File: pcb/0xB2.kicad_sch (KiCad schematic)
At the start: 40 parts, among them J1 USB_C_Receptacle_USB2.0, J2 Conn_01x12, J3 Conn_01x05, J4 Conn_01x12, J5 Conn_01x02, SW1 SW_Push, SW2 SW_Push, U1 RP2040, U2 GD25Q80CEIGR, U3 XC6210B332MR-G, Y1 Crystal_GND24

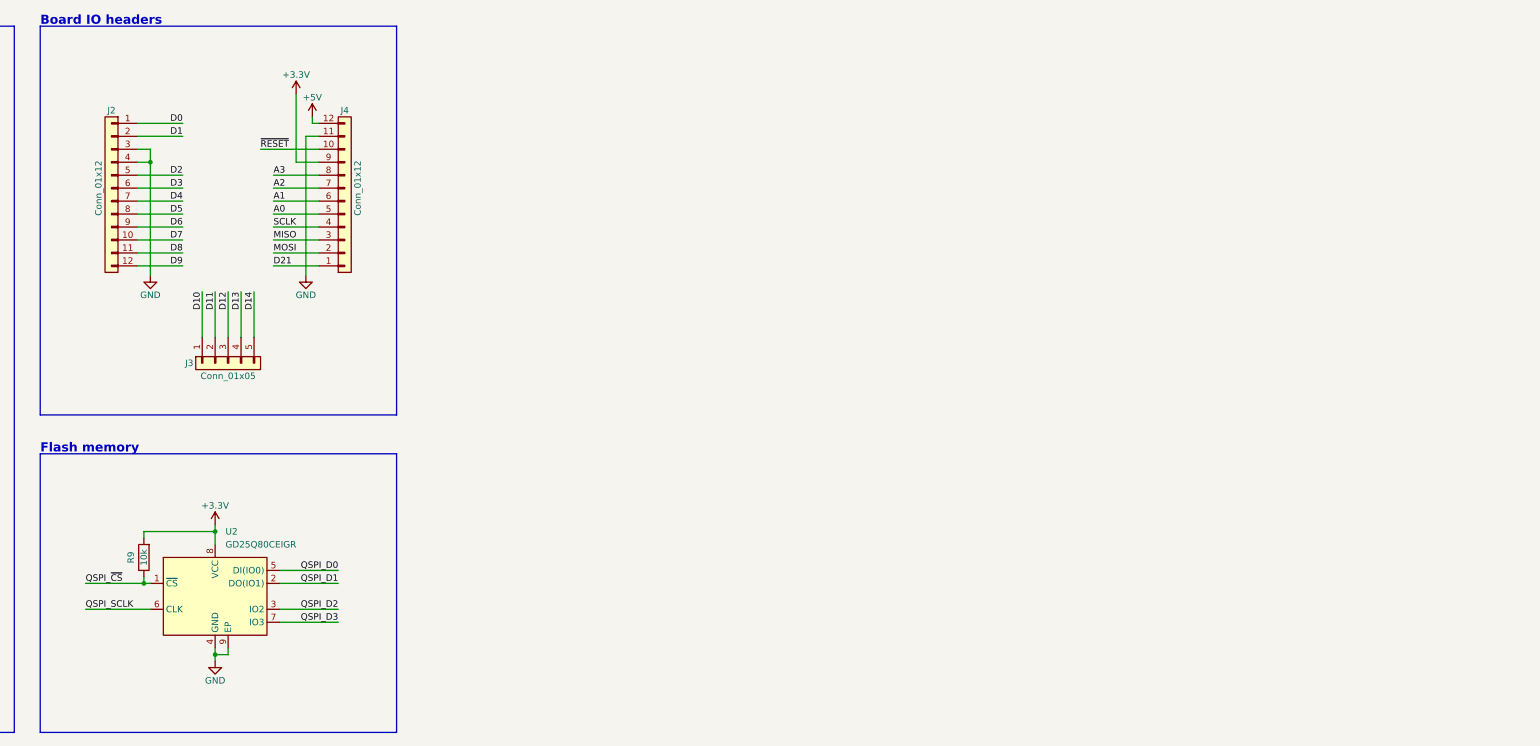
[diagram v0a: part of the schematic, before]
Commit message: add headers
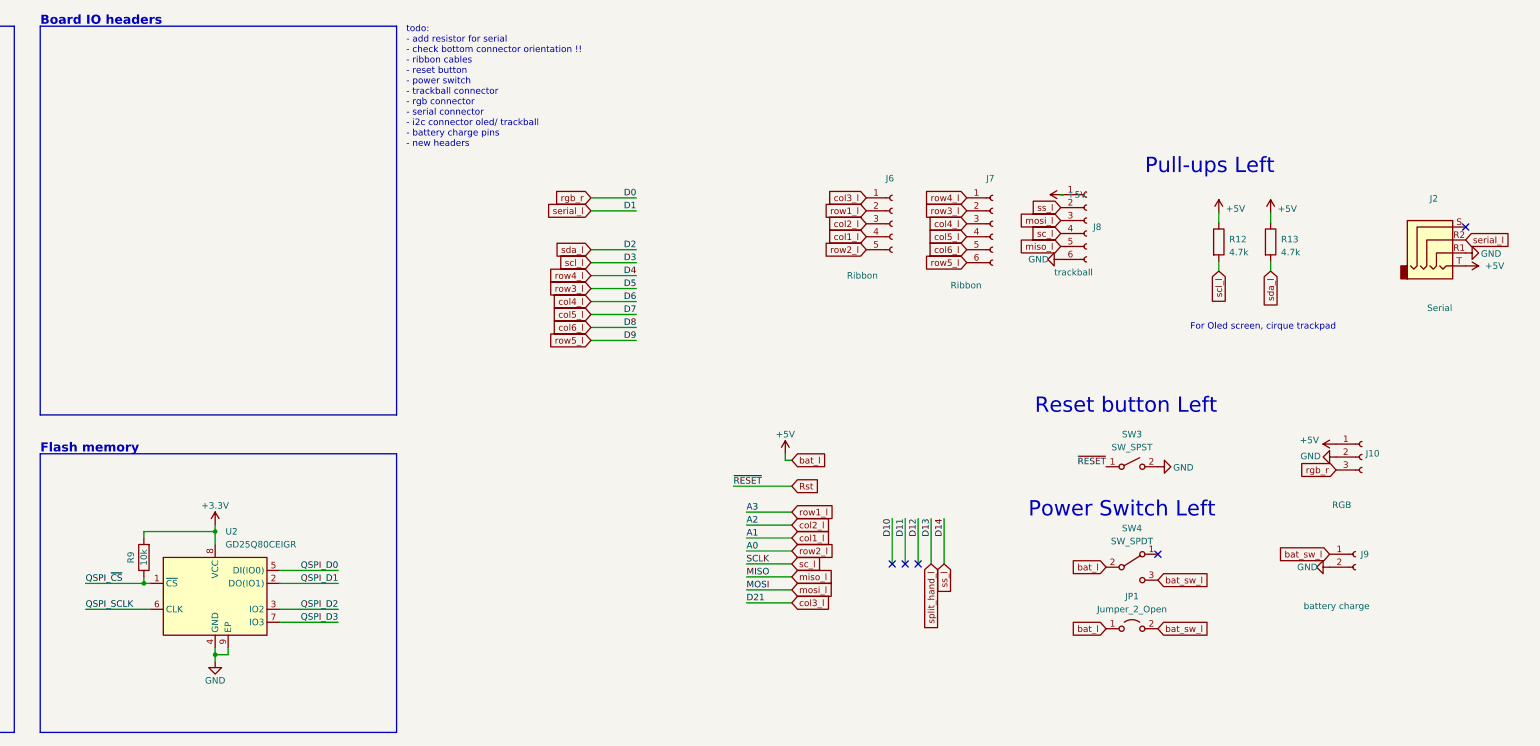
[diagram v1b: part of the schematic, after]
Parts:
- removed J2, J4: Conn_01x12, 0xLib_Connectors:PinHeader_1x12_P2.54mm, symbol Connector_Generic:Conn_01x12
- removed J3: Conn_01x05, 0xLib_Connectors:PinHeader_1x05_P2.54mm, symbol Connector_Generic:Conn_01x05
- added J10: RGB, Connector_PinHeader_2.54mm:PinHeader_1x03_P2.54mm_Vertical, symbol Connector:Conn_01x03_Female
- added J2: Serial, 0xB2_drawings:Jack_3.5mm_PJ320E_Horizontal, symbol Connector:AudioJack4
- added J6: Ribbon, Connector_PinHeader_2.54mm:PinHeader_1x05_P2.54mm_Vertical, symbol Connector:Conn_01x05_Female
- added J7: Ribbon, Connector_PinHeader_2.54mm:PinHeader_1x06_P2.54mm_Vertical, symbol Connector:Conn_01x06_Female
- added J8: trackball, Connector_PinHeader_2.54mm:PinHeader_1x06_P2.54mm_Vertical, symbol Connector:Conn_01x06_Female
- added J9: battery charge, Connector_PinHeader_2.54mm:PinHeader_1x02_P2.54mm_Vertical, symbol Connector:Conn_01x02_Female
- added JP1: Jumper_2_Open, Library:power_switch_jumper, symbol Jumper:Jumper_2_Open
- added R12, R13: 4.7k, Library:R_1206_handsolder, symbol Device:R
- added SW3: SW_SPST, Library:PushSwitch, symbol Switch:SW_SPST
- added SW4: SW_SPDT, Library:SW_SPDT+H-MSK12C01_hor(7pin_SMD), symbol Switch:SW_SPDT
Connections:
- net +5V: now also J10.1 (Pin_1), J2.T, J8.1 (Pin_1), JP1.1 (A), R12.1, R13.1, SW4.2 (B)
- net GND: now also J10.2 (Pin_2), J2.R1, J8.6 (Pin_6), J9.2 (Pin_2), SW3.2 (B)
- net A0 renamed row2_l
- net row2_l: now also J6.5 (Pin_5)
- net A1 renamed col1_l
- net col1_l: now also J6.4 (Pin_4)
- net A2 renamed col2_l
- net col2_l: now also J6.3 (Pin_3)
- net A3 renamed row1_l
- net row1_l: now also J6.2 (Pin_2)
- net D0 renamed rgb_r
- net rgb_r: now also J10.3 (Pin_3)
- net D1 renamed serial_l
- net serial_l: now also J2.R2
- net D13 renamed split_hand_l
- net D14 renamed ss_l
- net ss_l: now also J8.2 (Pin_2)
- net D2 renamed sda_l
- net sda_l: now also R13.2
- net D21 renamed col3_l
- net col3_l: now also J6.1 (Pin_1)
- net D3 renamed scl_l
- net scl_l: now also R12.2
- net D4 renamed row4_l
- net row4_l: now also J7.1 (Pin_1)
- net D5 renamed row3_l
- net row3_l: now also J7.2 (Pin_2)
- net D6 renamed col4_l
- net col4_l: now also J7.3 (Pin_3)
- net D7 renamed col5_l
- net col5_l: now also J7.4 (Pin_4)
- net D8 renamed col6_l
- net col6_l: now also J7.5 (Pin_5)
- net D9 renamed row5_l
- net row5_l: now also J7.6 (Pin_6)
- net MISO renamed miso_l
- net miso_l: now also J8.5 (Pin_5)
- net MOSI renamed mosi_l
- net mosi_l: now also J8.3 (Pin_3)
- net SCLK renamed sc_l
- net sc_l: now also J8.4 (Pin_4)
- net ~{RESET} renamed Rst
- net Rst: now also SW3.1 (A)
- new net bat_sw_l: J9.1 (Pin_1), JP1.2 (B), SW4.3 (C)
- no-connect marks 9 -> 14
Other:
- note added: "For Oled screen, cirque trackpad"
- note added: "Power Switch Left"
- note added: "Pull-ups Left"
- note added: "Reset button Left"
- note added: "todo: - add resistor for serial - check bottom connector orientation !! - ribbon cables - reset button - power switch - trackball connector - rgb connector - serial connector - i2c connector oled/ trackball - battery charge pins - new headers"

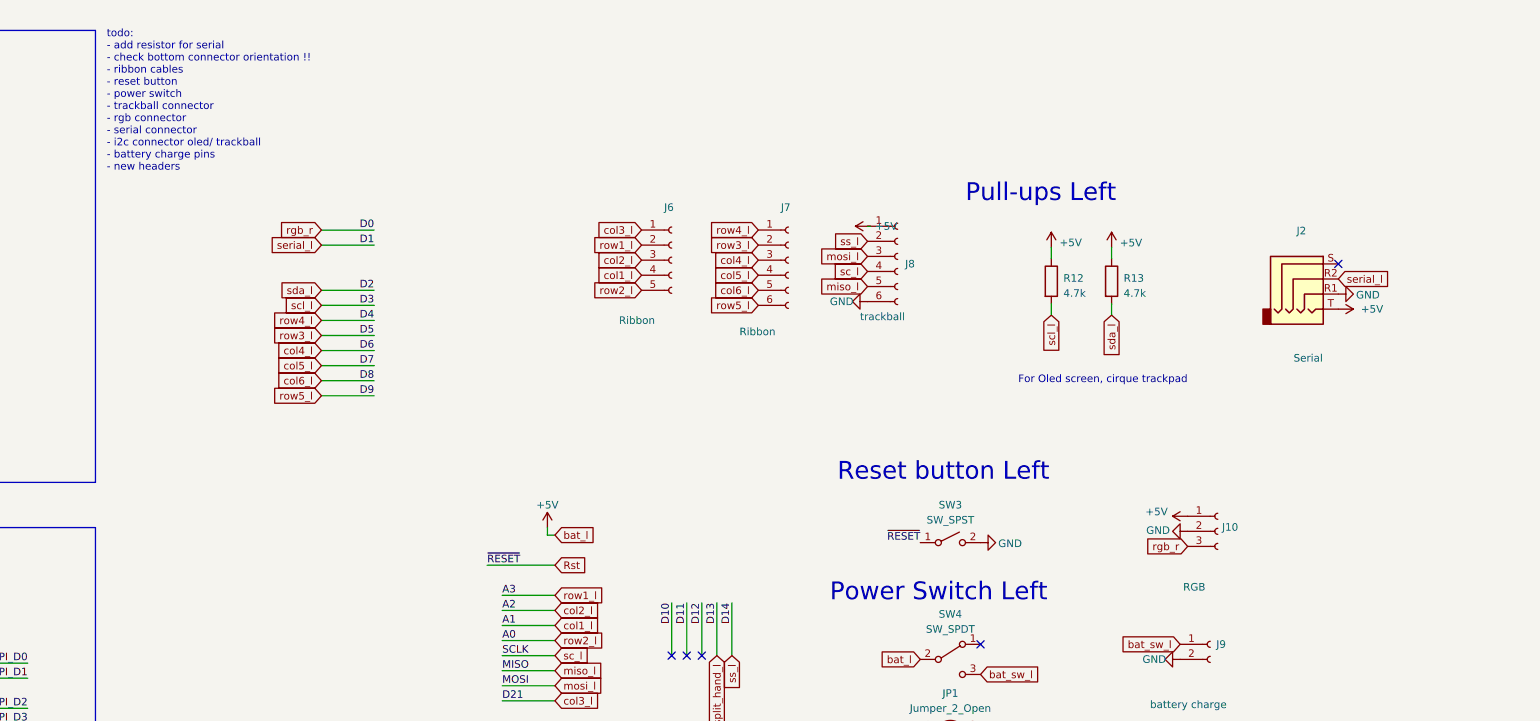
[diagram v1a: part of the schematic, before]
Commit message: add resistors
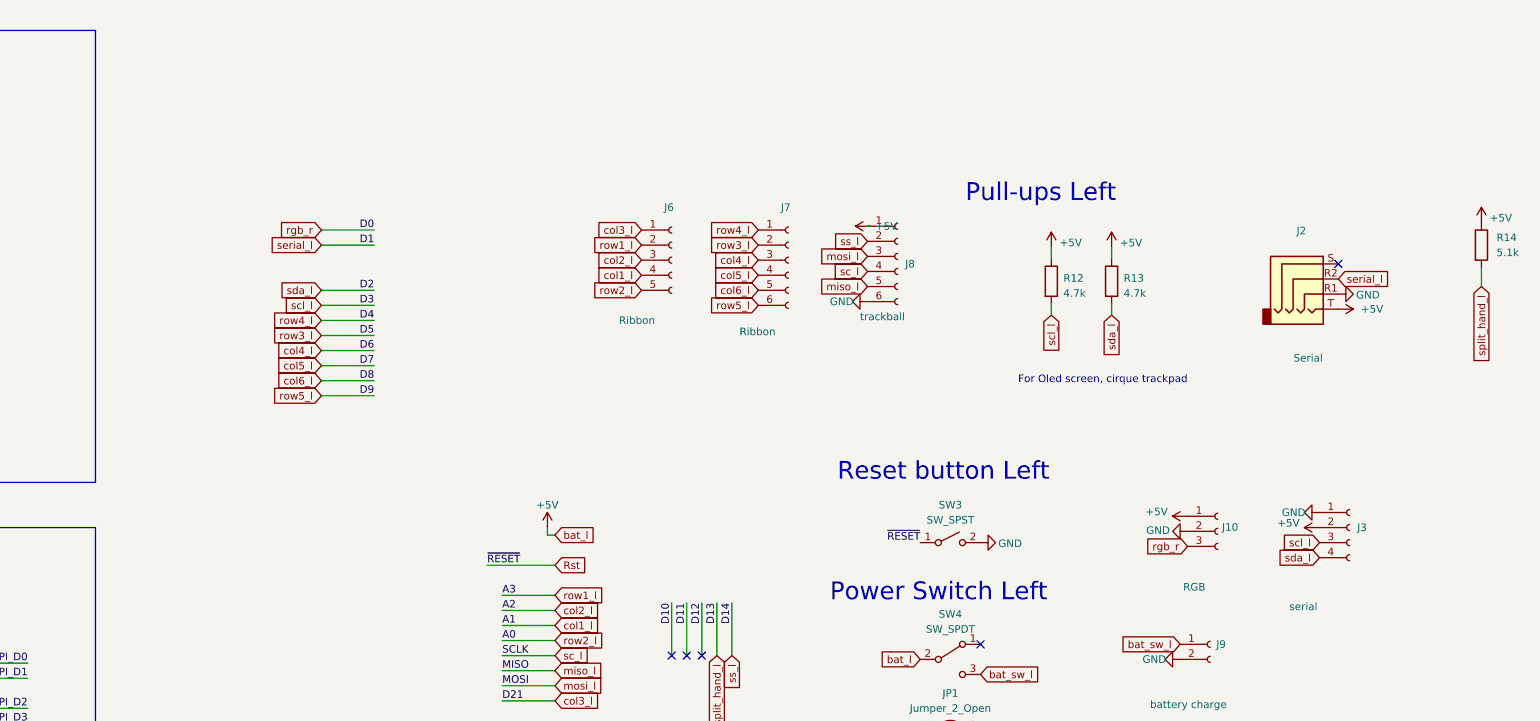
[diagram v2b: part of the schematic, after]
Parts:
- added J3: serial, Connector_PinHeader_2.54mm:PinHeader_1x04_P2.54mm_Vertical, symbol Connector:Conn_01x04_Female
- added R14: 5.1k, Resistor_SMD:R_0402_1005Metric, symbol Device:R
- R12, R13: footprint Library:R_1206_handsolder -> Resistor_SMD:R_0402_1005Metric
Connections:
- net +5V: now also J3.2 (Pin_2), R14.1
- net GND: now also J3.1 (Pin_1)
- net scl_l: now also J3.3 (Pin_3)
- net sda_l: now also J3.4 (Pin_4)
- net split_hand_l: now also R14.2
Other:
- note removed: "todo: - add resistor for serial - check bottom connector orientation !! - ribbon cables - reset button - power switch - trackball connector - rgb connector - serial connector - i2c connector oled/ trackball - battery charge pins - new headers"
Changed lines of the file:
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@@
+    (stroke (width 0) (type default) (color 0 0 0 0))
+  )
+  (wire (pts (xy 513.08 60.325) (xy 513.08 63.5))
     (stroke (width 0) (type default) (color 0 0 0 0))
   )
@@
   (text "Voltage regulation" (at 17.78 96.52 0)
     (effects (font (size 1.778 1.778) (thickness 0.3556) bold) (justify left bottom))
-  )
-  (text "todo:\n- add resistor for serial\n- check bottom connector orientation !!\n- ribbon cables\n- reset button\n- power switch\n- trackball connector \n- rgb connector\n- serial connector\n- i2c connector oled/ trackball\n- battery charge pins\n- new headers"
-    (at 281.305 44.196 0)
-    (effects (font (size 1.27 1.27)) (justify left bottom))
   )
   (text "Reset button Left" (at 404.495 96.52 0)
@@
     )
   )
+  (global_label "scl_l" (shape input) (at 485.775 106.68 180)
+    (effects (font (size 1.27 1.27)) (justify right))
+    (property "Intersheet References" "${INTERSHEET_REFS}" (id 0) (at 456.565 52.07 0)
+      (effects (font (size 1.27 1.27)) hide)
+    )
+  )
   (global_label "row1_l" (shape input) (at 371.475 56.515 180)
     (effects (font (size 1.27 1.27)) (justify right))
@@
     )
   )
+  (global_label "split_hand_l" (shape input) (at 513.08 63.5 270)
+    (effects (font (size 1.27 1.27)) (justify right))
+    (property "Intersheet References" "${INTERSHEET_REFS}" (id 0) (at 513.1594 75.6498 90)
+      (effects (font (size 1.27 1.27)) (justify right) hide)
+    )
+  )
   (global_label "bat_sw_l" (shape input) (at 428.625 138.43 0)
     (effects (font (size 1.27 1.27)) (justify left))
@@
     (property "Intersheet References" "${INTERSHEET_REFS}" (id 0) (at 405.1057 55.8006 0)
       (effects (font (size 1.27 1.27)) (justify right) hide)
+    )
+  )
+  (global_label "sda_l" (shape input) (at 485.775 109.22 180)
+    (effects (font (size 1.27 1.27)) (justify right))
+    (property "Intersheet References" "${INTERSHEET_REFS}" (id 0) (at 456.565 54.61 0)
+      (effects (font (size 1.27 1.27)) hide)
     )
   )
@@
       (effects (font (size 1.27 1.27)) hide)
     )
+  )
+  (symbol (lib_id "power:+5V") (at 485.775 104.14 90) (unit 1)
+    (in_bom yes) (on_board yes)
+    (property "Reference" "#PWR0115" (id 0) (at 489.585 104.14 0)
+      (effects (font (size 1.27 1.27)) hide)
+    )
+    (property "Value" "+5V" (id 1) (at 478.663 103.378 90)
+      (effects (font (size 1.27 1.27)) (justify right))
+    )
+    (property "Footprint" "" (id 2) (at 485.775 104.14 0)
+      (effects (font (size 1.27 1.27)) hide)
+    )
+    (property "Datasheet" "" (id 3) (at 485.775 104.14 0)
+      (effects (font (size 1.27 1.27)) hide)
+    )
+    (pin "1")
   )
   (symbol (lib_id "Device:C") (at 148.59 180.34 0) (unit 1)
@@
       (effects (font (size 1.27 1.27)) (justify left))
     )
-    (property "Footprint" "Library:R_1206_handsolder" (id 2) (at 438.785 62.611 90)
+    (property "Footprint" "Resistor_SMD:R_0402_1005Metric" (id 2) (at 438.785 62.611 90)
       (effects (font (size 1.27 1.27)) hide)
     )
@@
     (pin "2")
   )
+  (symbol (lib_id "Connector:Conn_01x04_Female") (at 490.855 104.14 0) (unit 1)
+    (in_bom yes) (on_board yes)
+    (property "Reference" "J3" (id 0) (at 492.125 104.1399 0)
+      (effects (font (size 1.27 1.27)) (justify left))
+    )
+    (property "Value" "serial" (id 1) (at 480.695 117.475 0)
+      (effects (font (size 1.27 1.27)) (justify left))
+    )
+    (property "Footprint" "Connector_PinHeader_2.54mm:PinHeader_1x04_P2.54mm_Vertical" (id 2) (at 490.855 104.14 0)
+      (effects (font (size 1.27 1.27)) hide)
+    )
+    (property "Datasheet" "~" (id 3) (at 490.855 104.14 0)
+      (effects (font (size 1.27 1.27)) hide)
+    )
+    (pin "1")
+    (pin "2")
+    (pin "3")
+    (pin "4")
+  )
   (symbol (lib_id "Device:R") (at 24.765 181.61 180) (unit 1)
     (in_bom yes) (on_board yes)
@@
     (pin "1")
   )
+  (symbol (lib_id "power:GND") (at 485.775 101.6 270) (unit 1)
+    (in_bom yes) (on_board yes)
+    (property "Reference" "#PWR0114" (id 0) (at 479.425 101.6 0)
+      (effects (font (size 1.27 1.27)) hide)
+    )
+    (property "Value" "GND" (id 1) (at 479.425 101.6 90)
+      (effects (font (size 1.27 1.27)) (justify left))
+    )
+    (property "Footprint" "" (id 2) (at 485.775 101.6 0)
+      (effects (font (size 1.27 1.27)) hide)
+    )
+    (property "Datasheet" "" (id 3) (at 485.775 101.6 0)
+      (effects (font (size 1.27 1.27)) hide)
+    )
+    (pin "1")
+  )
   (symbol (lib_id "Device:R") (at 450.723 62.611 0) (unit 1)
     (in_bom yes) (on_board yes)
@@
       (effects (font (size 1.27 1.27)) (justify left))
     )
-    (property "Footprint" "Library:R_1206_handsolder" (id 2) (at 448.945 62.611 90)
+    (property "Footprint" "Resistor_SMD:R_0402_1005Metric" (id 2) (at 448.945 62.611 90)
       (effects (font (size 1.27 1.27)) hide)
     )
@@
     (pin "2")
   )
+  (symbol (lib_id "power:+5V") (at 513.08 52.705 0) (unit 1)
+    (in_bom yes) (on_board yes)
+    (property "Reference" "#PWR0116" (id 0) (at 513.08 56.515 0)
+      (effects (font (size 1.27 1.27)) hide)
+    )
+    (property "Value" "+5V" (id 1) (at 514.477 51.943 0)
+      (effects (font (size 1.27 1.27)) (justify left))
+    )
+    (property "Footprint" "" (id 2) (at 513.08 52.705 0)
+      (effects (font (size 1.27 1.27)) hide)
+    )
+    (property "Datasheet" "" (id 3) (at 513.08 52.705 0)
+      (effects (font (size 1.27 1.27)) hide)
+    )
+    (pin "1")
+  )
   (symbol (lib_id "Device:C") (at 139.7 180.34 0) (unit 1)
     (in_bom yes) (on_board yes)
@@
     (pin "2")
   )
+  (symbol (lib_id "Device:R") (at 513.08 56.515 0) (unit 1)
+    (in_bom yes) (on_board yes)
+    (property "Reference" "R14" (id 0) (at 515.62 55.245 0)
+      (effects (font (size 1.27 1.27)) (justify left))
+    )
+    (property "Value" "5.1k" (id 1) (at 515.62 57.785 0)
+      (effects (font (size 1.27 1.27)) (justify left))
+    )
+    (property "Footprint" "Resistor_SMD:R_0402_1005Metric" (id 2) (at 511.302 56.515 90)
+      (effects (font (size 1.27 1.27)) hide)
+    )
+    (property "Datasheet" "~" (id 3) (at 513.08 56.515 0)
+      (effects (font (size 1.27 1.27)) hide)
+    )
+    (property "JLCPCB BOM" "1" (id 4) (at 513.08 56.515 0)
+      (effects (font (size 1.27 1.27)) hide)
+    )
+    (property "JLCPCB Part" "C26033" (id 5) (at 513.08 56.515 0)
+      (effects (font (size 1.27 1.27)) hide)
+    )
+    (pin "1")
+    (pin "2")
+  )
   (symbol (lib_id "power:+3.3V") (at 171.45 36.83 0) (unit 1)
     (in_bom yes) (on_board yes)
@@
       (reference "#PWR0113") (unit 1) (value "GND") (footprint "")
     )
+    (path "/8747965f-e8f1-436e-9771-3106e27614a4"
+      (reference "#PWR0114") (unit 1) (value "GND") (footprint "")
+    )
+    (path "/0147d85f-4d6f-4eb1-a523-7555cfa4d7f5"
+      (reference "#PWR0115") (unit 1) (value "+5V") (footprint "")
+    )
+    (path "/c4740c13-9da2-475c-b1bd-46fe95a7469f"
+      (reference "#PWR0116") (unit 1) (value "+5V") (footprint "")
+    )
     (path "/4a21e78b-0ab0-4b88-8132-9b174e045719"
       (reference "C1") (unit 1) (value "1µ") (footprint "Capacitor_SMD:C_0603_1608Metric")
@@
       (reference "J2") (unit 1) (value "Serial") (footprint "0xB2_drawings:Jack_3.5mm_PJ320E_Horizontal")
     )
+    (path "/7a7bc1c0-daf2-4628-9a90-84ea0eab7c8c"
+      (reference "J3") (unit 1) (value "serial") (footprint "Connector_PinHeader_2.54mm:PinHeader_1x04_P2.54mm_Vertical")
+    )
     (path "/06b6e523-10ae-4799-8871-3c7a3a700ad9"
       (reference "J5") (unit 1) (value "Conn_01x02") (footprint "Connector_PinHeader_1.27mm:PinHeader_1x02_P1.27mm_Vertical")
@@
     )
     (path "/2142cc0e-f6fe-43e7-979d-2e121cc9e2ce"
-      (reference "R12") (unit 1) (value "4.7k") (footprint "Library:R_1206_handsolder")
+      (reference "R12") (unit 1) (value "4.7k") (footprint "Resistor_SMD:R_0402_1005Metric")
     )
     (path "/87ab7132-6697-41dd-85f8-2a985e520eb7"
-      (reference "R13") (unit 1) (value "4.7k") (footprint "Library:R_1206_handsolder")
+      (reference "R13") (unit 1) (value "4.7k") (footprint "Resistor_SMD:R_0402_1005Metric")
+    )
+    (path "/e08a9b00-1e99-4e6b-b7b2-1cad9e7d687f"
+      (reference "R14") (unit 1) (value "5.1k") (footprint "Resistor_SMD:R_0402_1005Metric")
     )
     (path "/c30a3276-ac5c-4a68-880e-26478e1b53e4"

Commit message: usb c work
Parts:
- removed J9: battery charge, Connector_PinHeader_2.54mm:PinHeader_1x02_P2.54mm_Vertical, symbol Connector:Conn_01x02_Female
- added J?: usb_shield2, Connector_PinHeader_2.54mm:PinHeader_1x02_P2.54mm_Vertical, symbol Connector:Conn_01x02_Female
- added J?: usb_shield1, Connector_PinHeader_2.54mm:PinHeader_1x02_P2.54mm_Vertical, symbol Connector:Conn_01x02_Female
- added J?: usb_daughter2, Connector_PinHeader_2.54mm:PinHeader_1x02_P2.54mm_Vertical, symbol Connector:Conn_01x02_Female
- added J?: usb_daughter1, Connector_PinHeader_2.54mm:PinHeader_1x02_P2.54mm_Vertical, symbol Connector:Conn_01x02_Female
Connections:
- net +3V3: now also R12.1, R13.1, R14.1
- net +5V: now also J?.2 (Pin_2); no longer R12.1, R13.1, R14.1
- net D+: now also J?.2 (Pin_2); no longer J1.A6 (D+), J1.B6 (D+)
- net D-: now also J?.1 (Pin_1); no longer J1.A7 (D-), J1.B7 (D-)
- net GND: now also J?.1 (Pin_1)
- new net D+_daughter: J1.A6 (D+), J1.B6 (D+), J?.2 (Pin_2)
- new net D-_daughter: J1.A7 (D-), J1.B7 (D-), J?.1 (Pin_1)
- new net Gnd_daugther: J?.1 (Pin_1)
- new net Vcc_daugther: J?.2 (Pin_2)
